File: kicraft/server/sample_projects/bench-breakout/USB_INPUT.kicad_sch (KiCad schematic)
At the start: 5 parts, among them J1 USB-C Receptacle

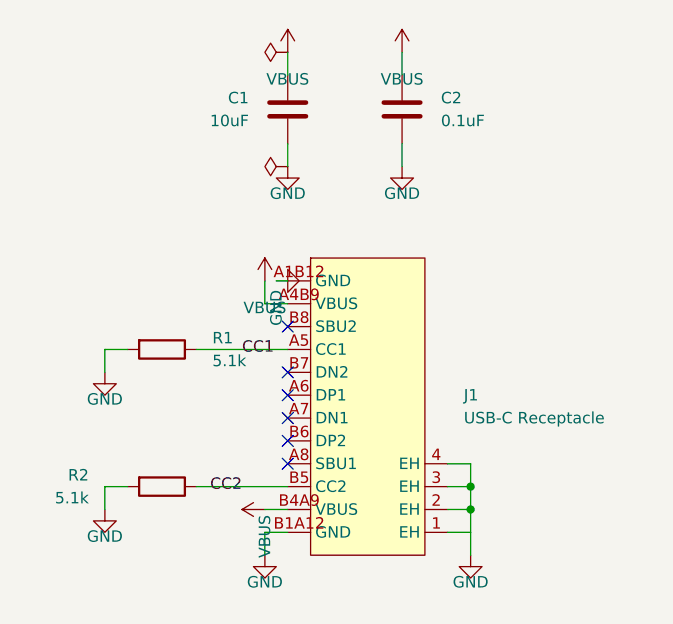
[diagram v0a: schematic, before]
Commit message: feat(showcase): refresh landing samples from self-eval 20260614
Promote the three best boards from self-eval batch 20260614T215540Z
(all grade B) into the landing-page showcase, replacing the regressed
PIR night light (D/45, hit erc_errors + unprogrammable_mcu gates):

- usb-pd-trigger (NEW, featured hero) — 81.0, fab-ready
- weather-sensor (re-promoted; stem A_BMP280_BAROMETRIC -> BMP280_QWIIC_USB_C)
- bench-breakout (re-promoted; 4->5 sheets, 16->19 parts)

Regenerated board.png/hero.png renders and interactive board.glb models
via scripts/promote_to_sample.py. Already live (deploy/restart-web.sh).

Co-Authored-By: Claude Opus 4.8 (1M context) <noreply@anthropic.com>
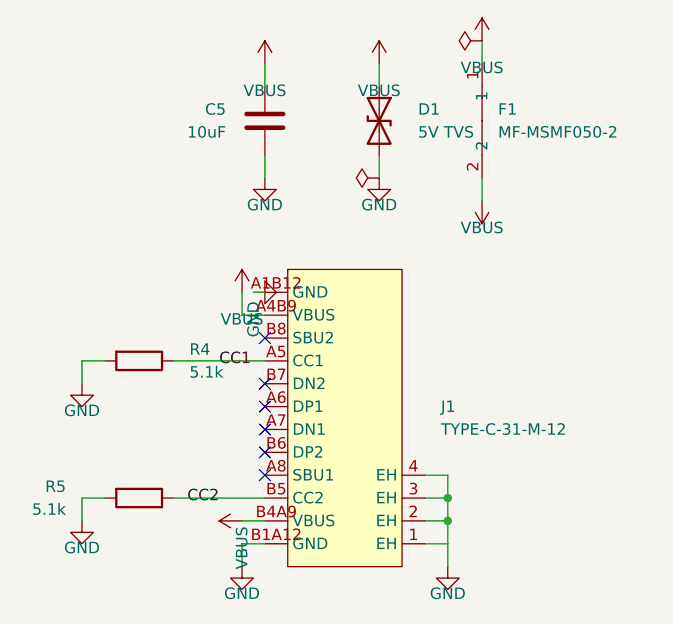
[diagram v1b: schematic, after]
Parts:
- removed C1: 10uF, Capacitor_SMD:C_0805_2012Metric, symbol Device:C
- removed C2: 0.1uF, Capacitor_SMD:C_0805_2012Metric, symbol Device:C
- removed R1, R2: 5.1k, Resistor_SMD:R_0805_2012Metric, symbol Device:R
- added C5: 10uF, Capacitor_SMD:C_0805_2012Metric, symbol Device:C
- added D1: 5V TVS, Diode_SMD:D_SOD-123, symbol Device:D_TVS
- added F1: MF-MSMF050-2, mf-msmf050-2:F1812, symbol mf-msmf050-2:MF-MSMF050-2
- added R4, R5: 5.1k, Resistor_SMD:R_0805_2012Metric, symbol Device:R
- J1: value USB-C Receptacle -> TYPE-C-31-M-12
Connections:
- net CC1: now also R4.1
- net CC2: now also R5.1
- net GND: now also C5.2, D1.2 (A2), R4.2, R5.2
- net VBUS: now also C5.1, D1.1 (A1), F1.1, F1.2
